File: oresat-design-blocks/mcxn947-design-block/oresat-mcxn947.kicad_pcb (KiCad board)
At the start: 4 copper layers, 73.1 x 69.8 mm, 83 parts, among them J1 BKUP-BATT, J10 Conn_02x20_Odd_Even, J2 USB_C_Receptacle_USB2.0_14P, J3 CAN, J4 TERM, J5 10pin ARM SWD, J6 FTDI-UART-6PIN, J7 OreSat Debug, J9 Conn_02x20_Odd_Even, SW1 RESET, SW2 ISP(BOOT), U1 MCXN947VKLT, U2 TCAN330, U3 TPS62111RSA, Y1 24 MHz, Y2 32.768 KHz

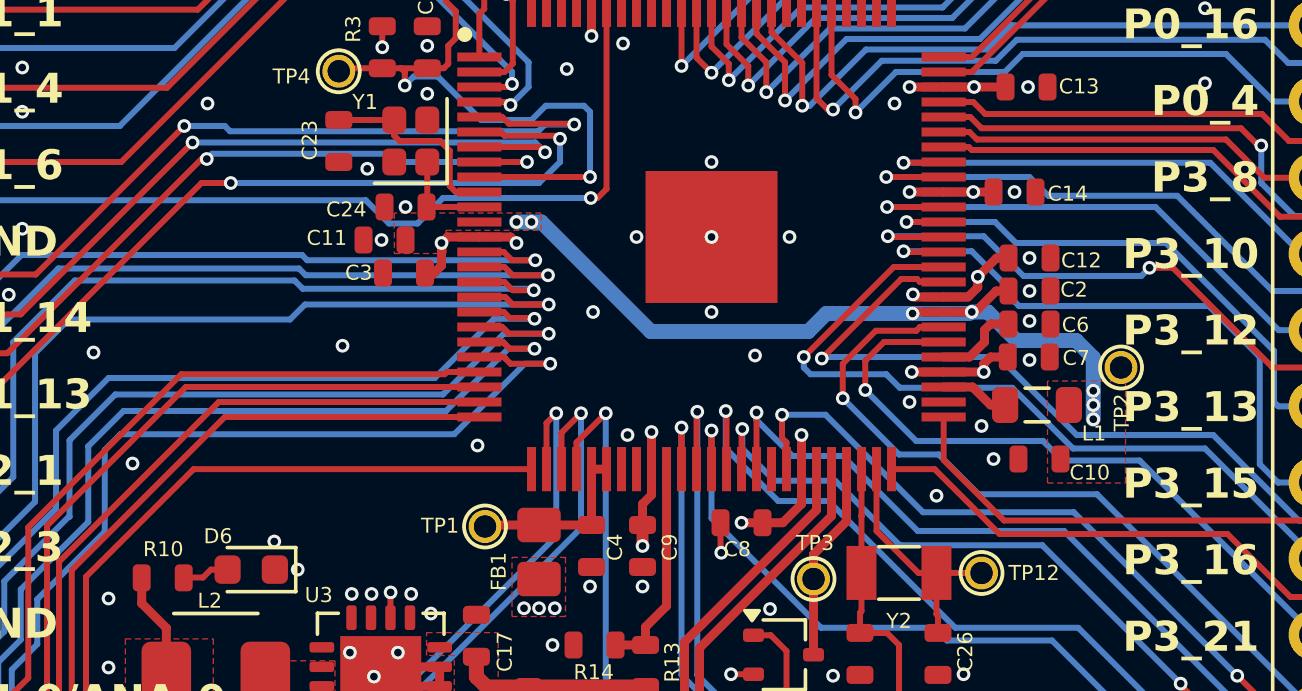
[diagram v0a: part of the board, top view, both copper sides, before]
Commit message: Updated BOM with distributor part numbers, lots of double checking. Now truly version 1.1
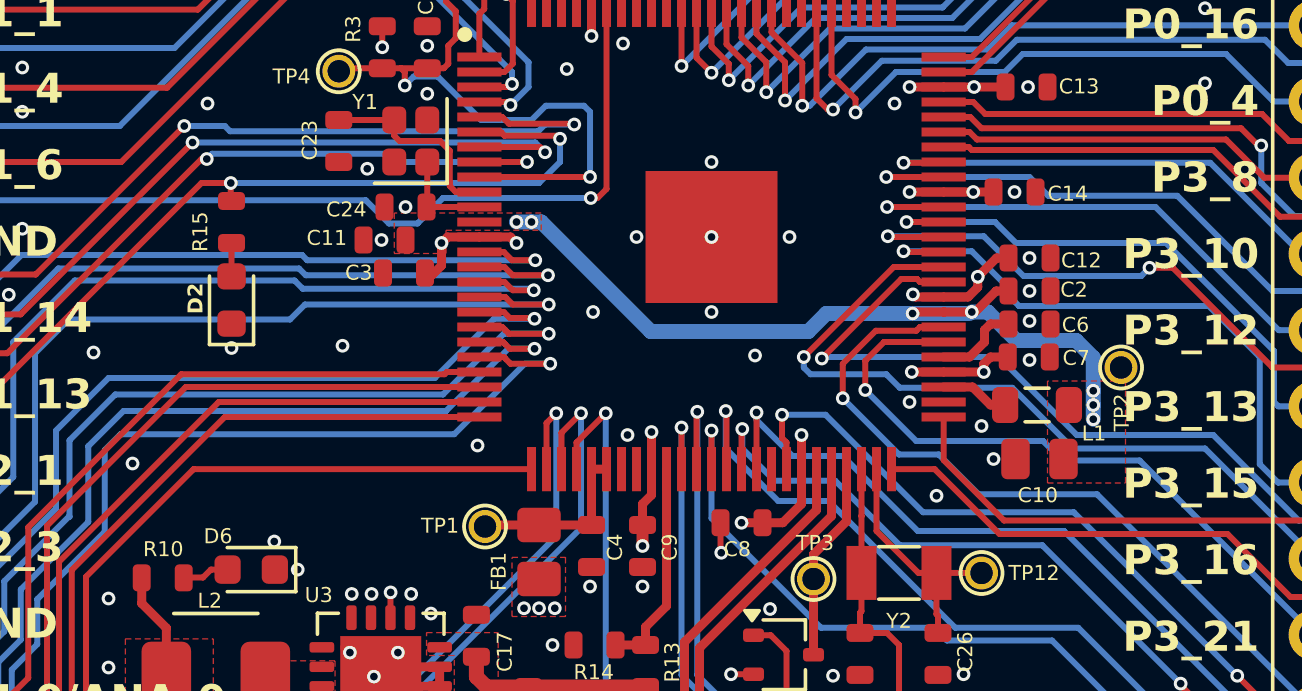
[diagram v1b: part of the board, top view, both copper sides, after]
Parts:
- added D2: AMBER, LED_SMD:LED_0603_1608Metric, F.Cu at (144.5, 102.8)
- added R15: 5.11k, oresat-passives:0603-C-NOSILK, F.Cu at (144.5, 100.2)
- C10: footprint oresat-passives:0603-C-NOSILK -> oresat-passives:0805-C-NOSILK
- D6: value GREEN -> GRN
- R10: value 10k -> 5.11k
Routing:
- net Net-(D2-A): track 0.00 -> 1.11 mm
- net P1_13: track 28.5 -> 29.1 mm
- net GND: vias 140 -> 141
